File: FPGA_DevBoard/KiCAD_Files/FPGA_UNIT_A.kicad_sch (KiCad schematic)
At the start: 43 parts, among them U19 XC7S50-1FTGB196C, U2 ASEM1-100.000MHZ-LC-T

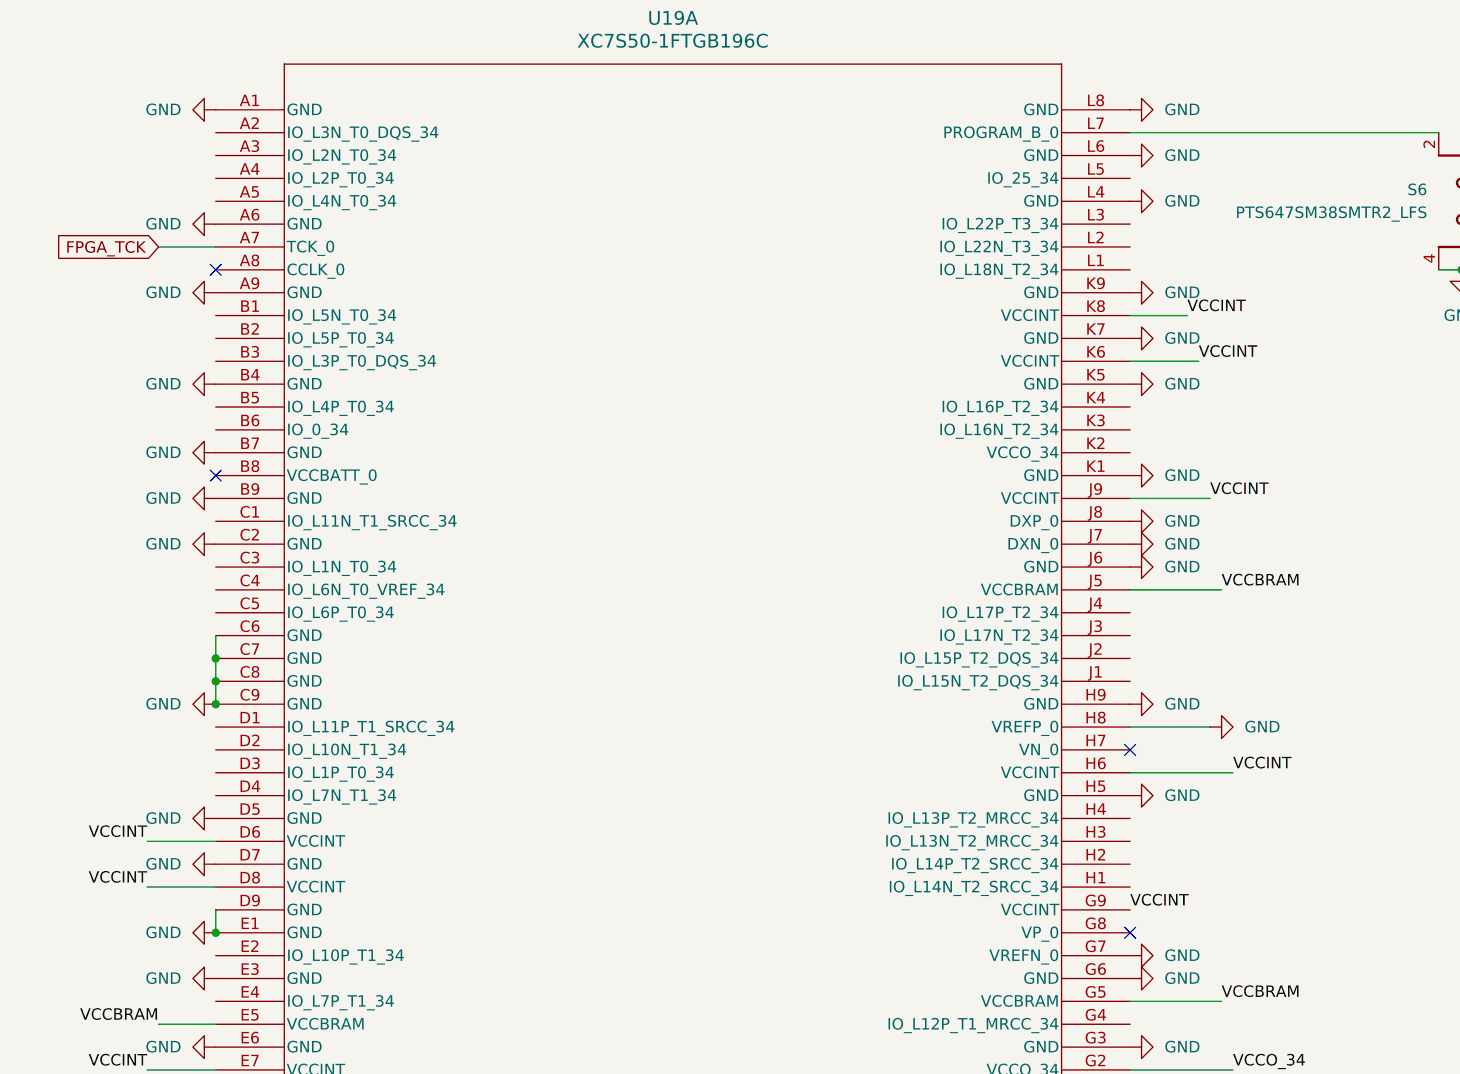
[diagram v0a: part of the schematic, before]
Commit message: ESD
Added ESD to the main USB programmer. Also added terminating resistors and test points. Also updated some planes to make sure everything was connected.
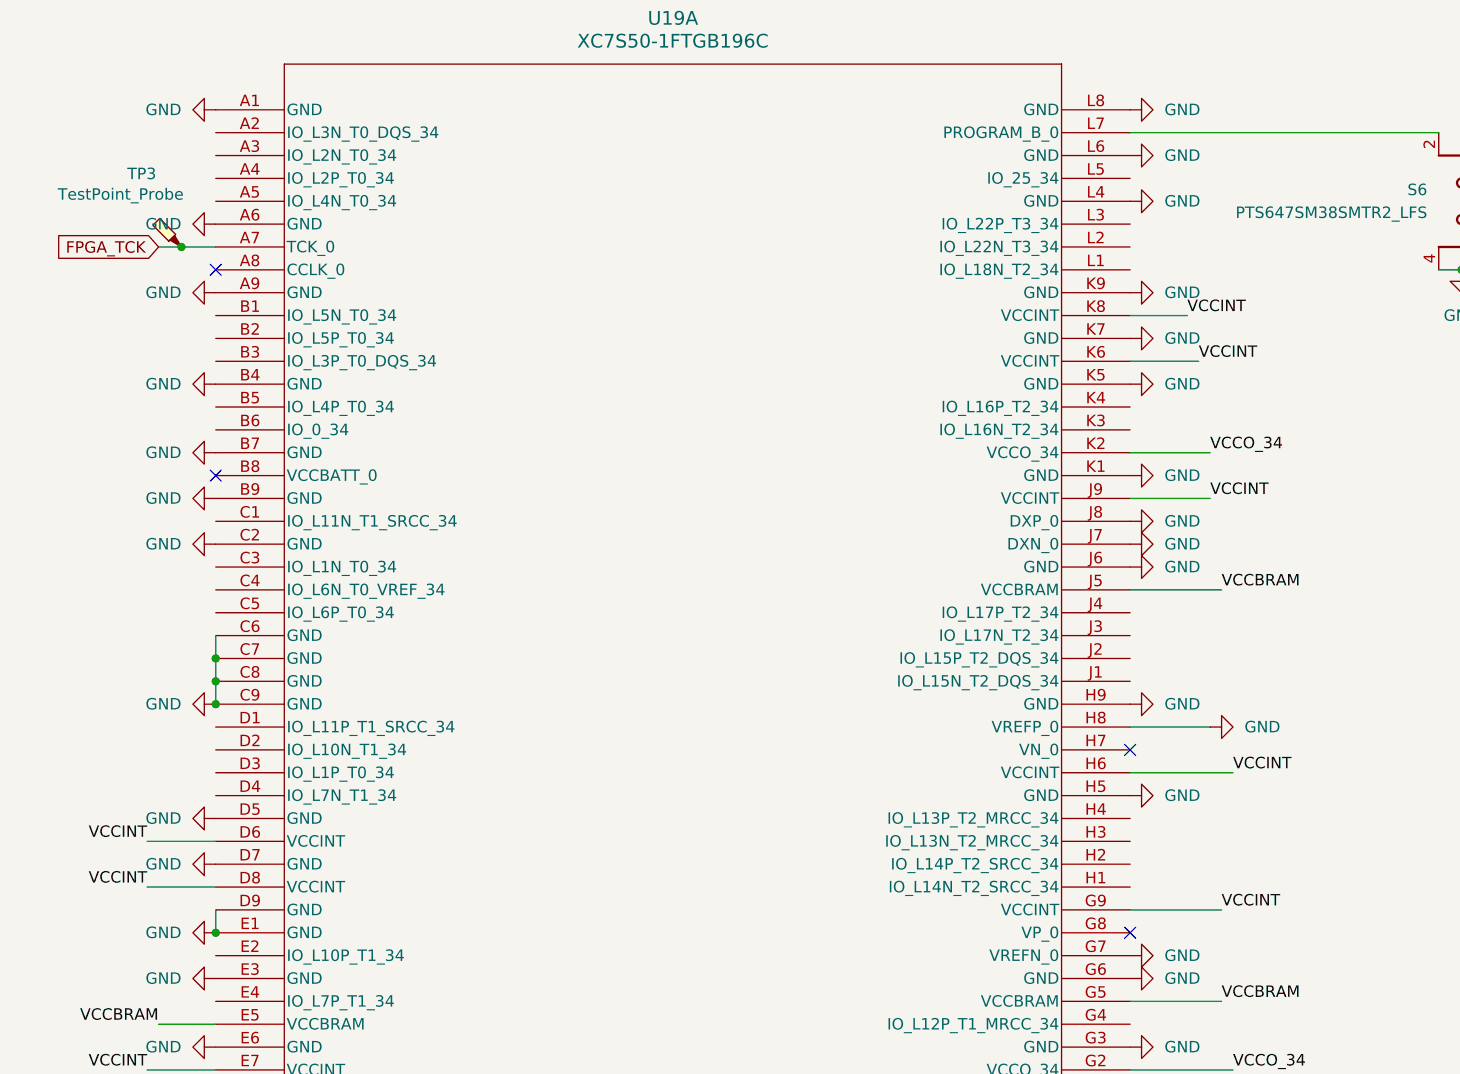
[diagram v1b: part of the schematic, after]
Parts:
- added TP3: TestPoint_Probe, TestPoint:TestPoint_Pad_D1.0mm, symbol Connector:TestPoint_Probe
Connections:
- net +3V3: now also U19.K2 (VCCO_34)
- net FPGA_TCK: now also TP3.1
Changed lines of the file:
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@@
+	)
+	(junction
+		(at 24.13 38.1)
+		(diameter 0)
+		(color 0 0 0 0)
 	)
 	(junction
@@
 	(wire
 		(pts
+			(xy 24.13 38.1) (xy 27.94 38.1)
+		)
+		(stroke
+			(width 0)
+			(type default)
+		)
+	)
+	(wire
+		(pts
 			(xy 43.18 196.85) (xy 31.75 196.85)
 		)
@@
 	(wire
 		(pts
+			(xy 138.43 60.96) (xy 129.54 60.96)
+		)
+		(stroke
+			(width 0)
+			(type default)
+		)
+	)
+	(wire
+		(pts
 			(xy 45.72 210.82) (xy 59.69 210.82)
 		)
@@
 	(wire
 		(pts
+			(xy 139.7 111.76) (xy 129.54 111.76)
+		)
+		(stroke
+			(width 0)
+			(type default)
+		)
+	)
+	(wire
+		(pts
 			(xy 100.33 256.54) (xy 113.03 256.54)
 		)
@@
 	(wire
 		(pts
-			(xy 21.59 38.1) (xy 27.94 38.1)
+			(xy 21.59 38.1) (xy 24.13 38.1)
 		)
 		(stroke
@@
 		)
 	)
+	(label "VCCO_34"
+		(at 138.43 60.96 0)
+		(effects
+			(font
+				(size 1.27 1.27)
+			)
+			(justify left bottom)
+		)
+	)
 	(label "VCCBRAM"
 		(at 139.7 76.2 0)
@@
 	)
 	(label "VCCINT"
-		(at 129.54 111.76 0)
+		(at 139.7 111.76 0)
 		(effects
 			(font
@@
 					(unit 1)
 				)
+			)
+		)
+	)
+	(symbol
+		(lib_id "Connector:TestPoint_Probe")
+		(at 24.13 38.1 0)
+		(mirror y)
+		(unit 1)
+		(exclude_from_sim no)
+		(in_bom yes)
+		(on_board yes)
+		(dnp no)
+		(property "Reference" "TP3"
+			(at 21.336 29.972 0)
+			(effects
+				(font
+					(size 1.27 1.27)
+				)
+				(justify left)
+			)
+		)
+		(property "Value" "TestPoint_Probe"
+			(at 24.384 32.258 0)
+			(effects
+				(font
+					(size 1.27 1.27)
+				)
+				(justify left)
+			)
+		)
+		(property "Footprint" "TestPoint:TestPoint_Pad_D1.0mm"
+			(at 19.05 38.1 0)
+			(effects
+				(font
+					(size 1.27 1.27)
+				)
+				(hide yes)
+			)
+		)
+		(property "Datasheet" "~"
+			(at 19.05 38.1 0)
+			(effects
+				(font
+					(size 1.27 1.27)
+				)
+				(hide yes)
+			)
+		)
+		(property "Description" "test point (alternative probe-style design)"
+			(at 24.13 38.1 0)
+			(effects
+				(font
+					(size 1.27 1.27)
+				)
+				(hide yes)
+			)
+		)
+		(pin "1"
+		)
+		(instances
+			(project "FPGA_DevBoard"
+				(path "/29dacc10-fb0d-42da-8b4b-fe903faf3f1a/f7a80be1-c773-4d61-a2a3-9f7c03a69ae0"
+					(reference "TP3")
+					(unit 1)
+				)

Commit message: Final updates
Draft 1 Finished!
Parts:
- R40: value 1k -> 4.7k
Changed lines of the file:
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@@
 			)
 		)
-		(property "Value" "1k"
+		(property "Value" "4.7k"
 			(at 180.34 24.384 90)
 			(effects

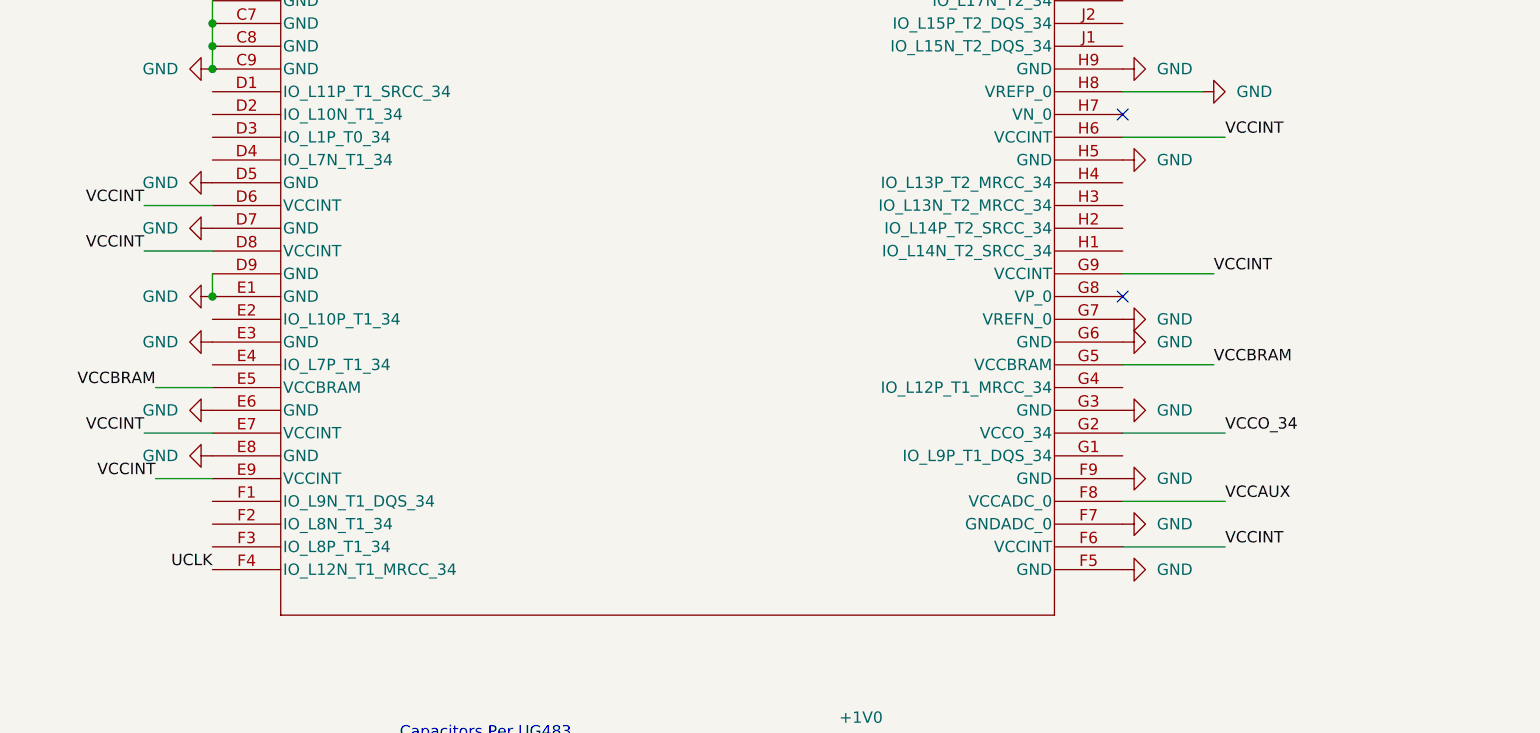
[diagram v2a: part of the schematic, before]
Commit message: Updated the NBSB IO to not go to input only, need to change this on the layout. Updated the FPGA clk to go to a positive differential signal with MCRR - need to change on layout. Updated the USB-UART bridge to not have Regin grounded - need to change on layout.
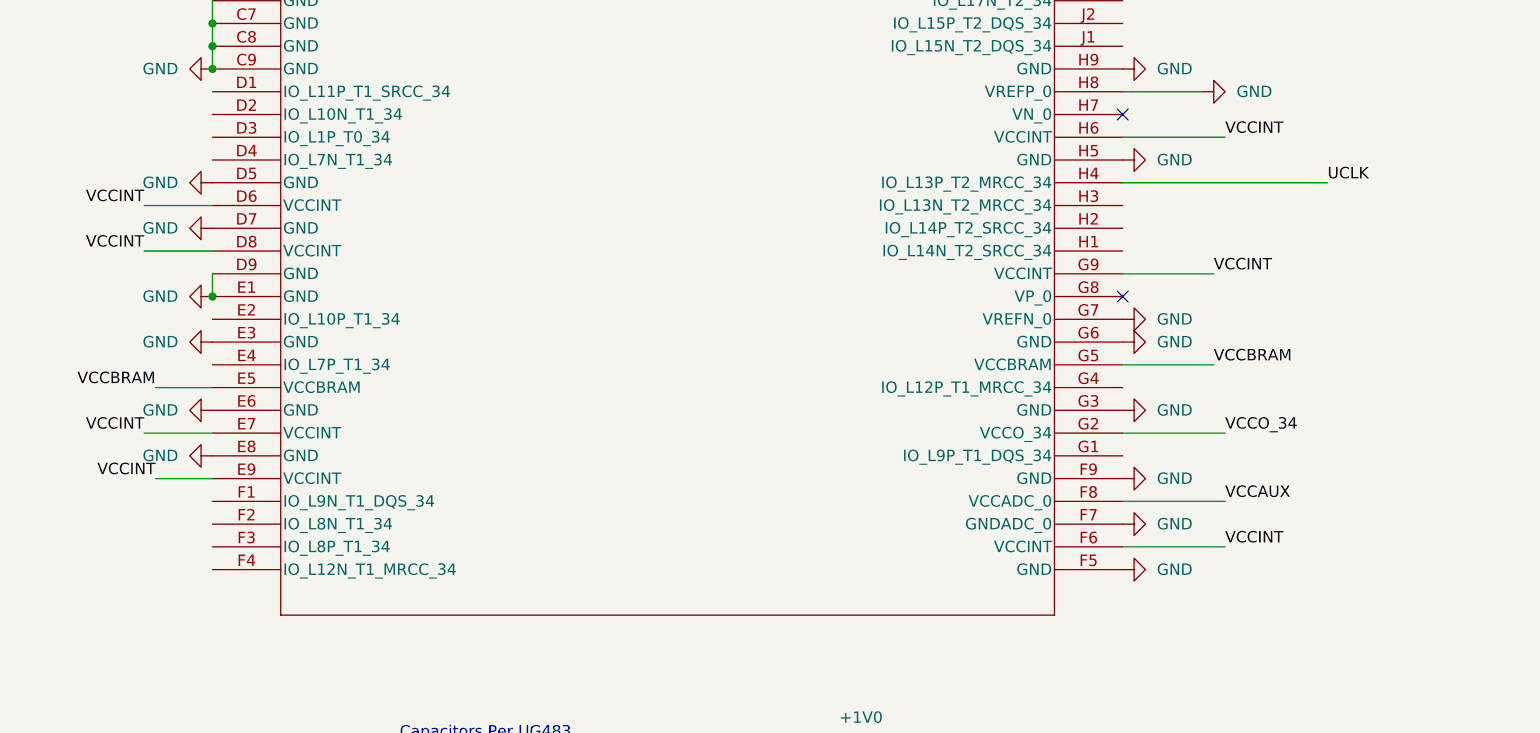
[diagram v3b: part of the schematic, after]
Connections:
- net UCLK: now also U19.H4 (IO_L13P_T2_MRCC_34); no longer U19.F4 (IO_L12N_T1_MRCC_34)

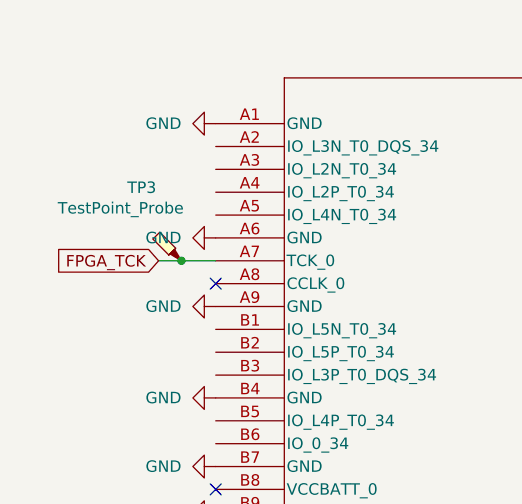
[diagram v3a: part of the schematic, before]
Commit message: Updated the layout to remove the JTAG header, connect the proper lines for the UART, and connect the proper pins for the audio.
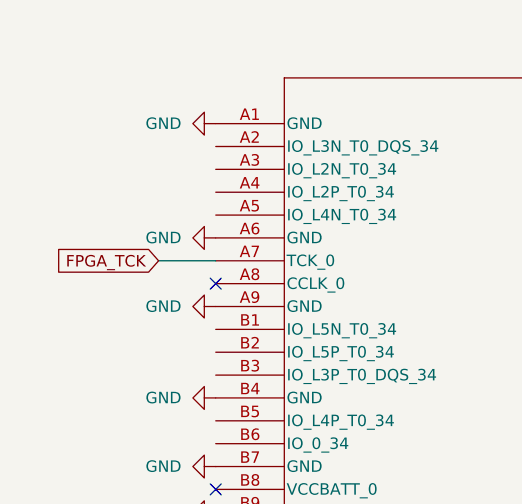
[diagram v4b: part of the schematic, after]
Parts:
- removed TP3: TestPoint_Probe, TestPoint:TestPoint_Pad_D1.0mm, symbol Connector:TestPoint_Probe
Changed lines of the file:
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@@
 	)
 	(junction
-		(at 24.13 38.1)
-		(diameter 0)
-		(color 0 0 0 0)
-	)
-	(junction
 		(at 113.03 203.2)
 		(diameter 0)
@@
 	(wire
 		(pts
-			(xy 24.13 38.1) (xy 27.94 38.1)
-		)
-		(stroke
-			(width 0)
-			(type default)
-		)
-	)
-	(wire
-		(pts
 			(xy 43.18 196.85) (xy 31.75 196.85)
 		)
@@
 	(wire
 		(pts
-			(xy 21.59 38.1) (xy 24.13 38.1)
+			(xy 21.59 38.1) (xy 27.94 38.1)
 		)
 		(stroke
@@
 					(unit 1)
 				)
-			)
-		)
-	)
-	(symbol
-		(lib_id "Connector:TestPoint_Probe")
-		(at 24.13 38.1 0)
-		(mirror y)
-		(unit 1)
-		(body_style 1)
-		(exclude_from_sim no)
-		(in_bom yes)
-		(on_board yes)
-		(in_pos_files yes)
-		(dnp no)
-		(property "Reference" "TP3"
-			(at 21.336 29.972 0)
-			(show_name no)
-			(do_not_autoplace no)
-			(effects
-				(font
-					(size 1.27 1.27)
-				)
-				(justify left)
-			)
-		)
-		(property "Value" "TestPoint_Probe"
-			(at 24.384 32.258 0)
-			(show_name no)
-			(do_not_autoplace no)
-			(effects
-				(font
-					(size 1.27 1.27)
-				)
-				(justify left)
-			)
-		)
-		(property "Footprint" "TestPoint:TestPoint_Pad_D1.0mm"
-			(at 19.05 38.1 0)
-			(hide yes)
-			(show_name no)
-			(do_not_autoplace no)
-			(effects
-				(font
-					(size 1.27 1.27)
-				)
-			)
-		)
-		(property "Datasheet" ""
-			(at 19.05 38.1 0)
-			(hide yes)
-			(show_name no)
-			(do_not_autoplace no)
-			(effects
-				(font
-					(size 1.27 1.27)
-				)
-			)
-		)
-		(property "Description" "test point (alternative probe-style design)"
-			(at 24.13 38.1 0)
-			(hide yes)
-			(show_name no)
-			(do_not_autoplace no)
-			(effects
-				(font
-					(size 1.27 1.27)
-				)
-			)
-		)
-		(pin "1"
-		)
-		(instances
-			(project "FPGA_DevBoard"
-				(path "/29dacc10-fb0d-42da-8b4b-fe903faf3f1a/f7a80be1-c773-4d61-a2a3-9f7c03a69ae0"
-					(reference "TP3")
-					(unit 1)
-				)

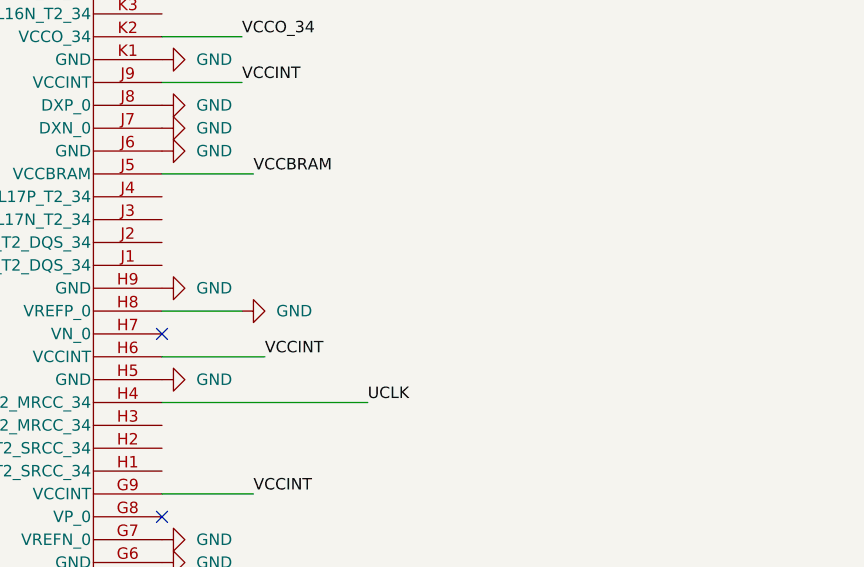
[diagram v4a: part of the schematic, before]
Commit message: Universal Serial Bussin it down
Replaced the USB Hub with the new USB Hosts, added a clock reset button, moved some things on the silk screen.
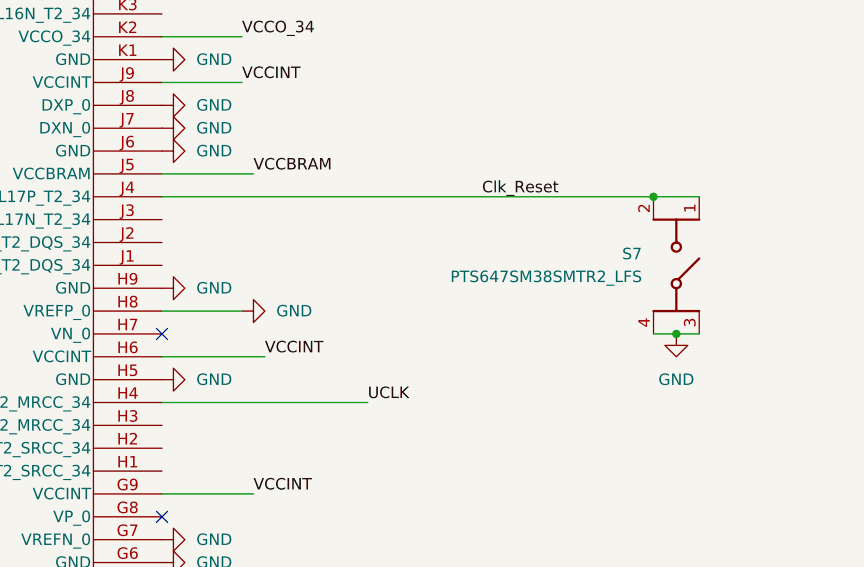
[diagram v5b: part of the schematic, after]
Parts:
- added S7: PTS647SM38SMTR2_LFS, FPGA_Interface:PTS647SM38SMTR2LFS, symbol FPGA_Interface:PTS647SM38SMTR2_LFS
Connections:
- net GND: now also S7.3 (COM_1), S7.4 (COM_2)
- net Clk_Reset: now reaches U19.J4 (IO_L17P_T2_34)
- net Clk_Reset: now also S7.1 (NO_1), S7.2 (NO_2)
